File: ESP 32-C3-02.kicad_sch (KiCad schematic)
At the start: 24 parts, among them J3 GSD090012SEU, U2 ESP32-C3-WROOM-02-H4, U3 CP2102N-Axx-xQFN20, U4 W25Q32JVSSIQ, U5 USBLC6-2SC6

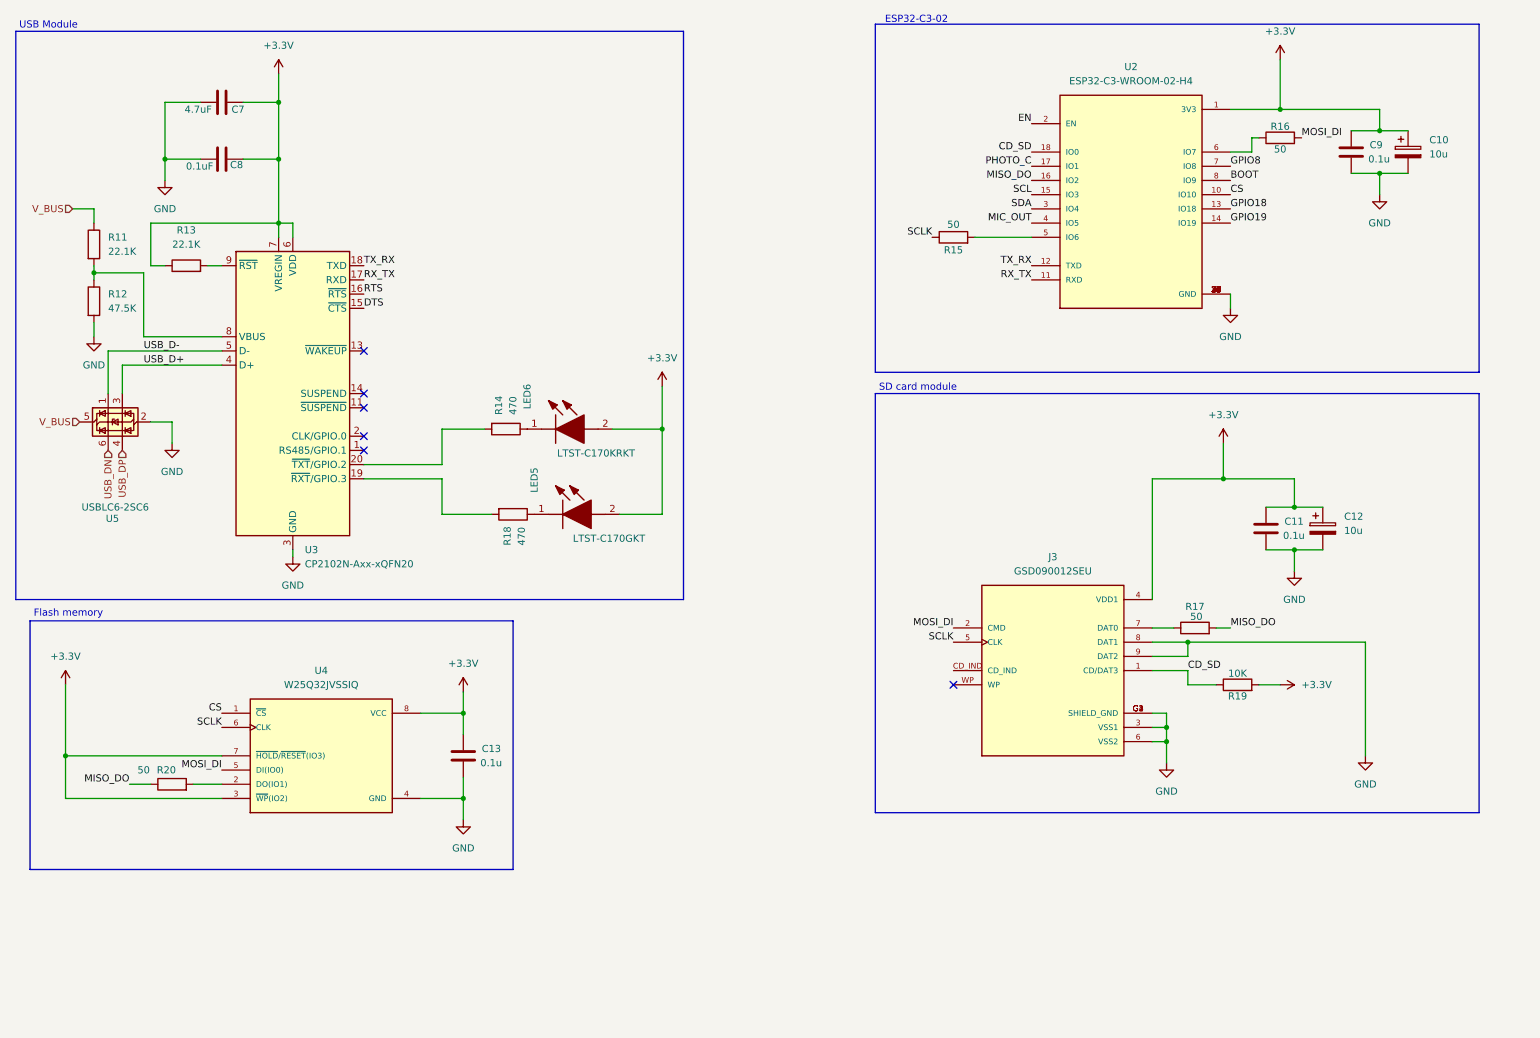
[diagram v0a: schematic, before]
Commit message: test point added to the schematics
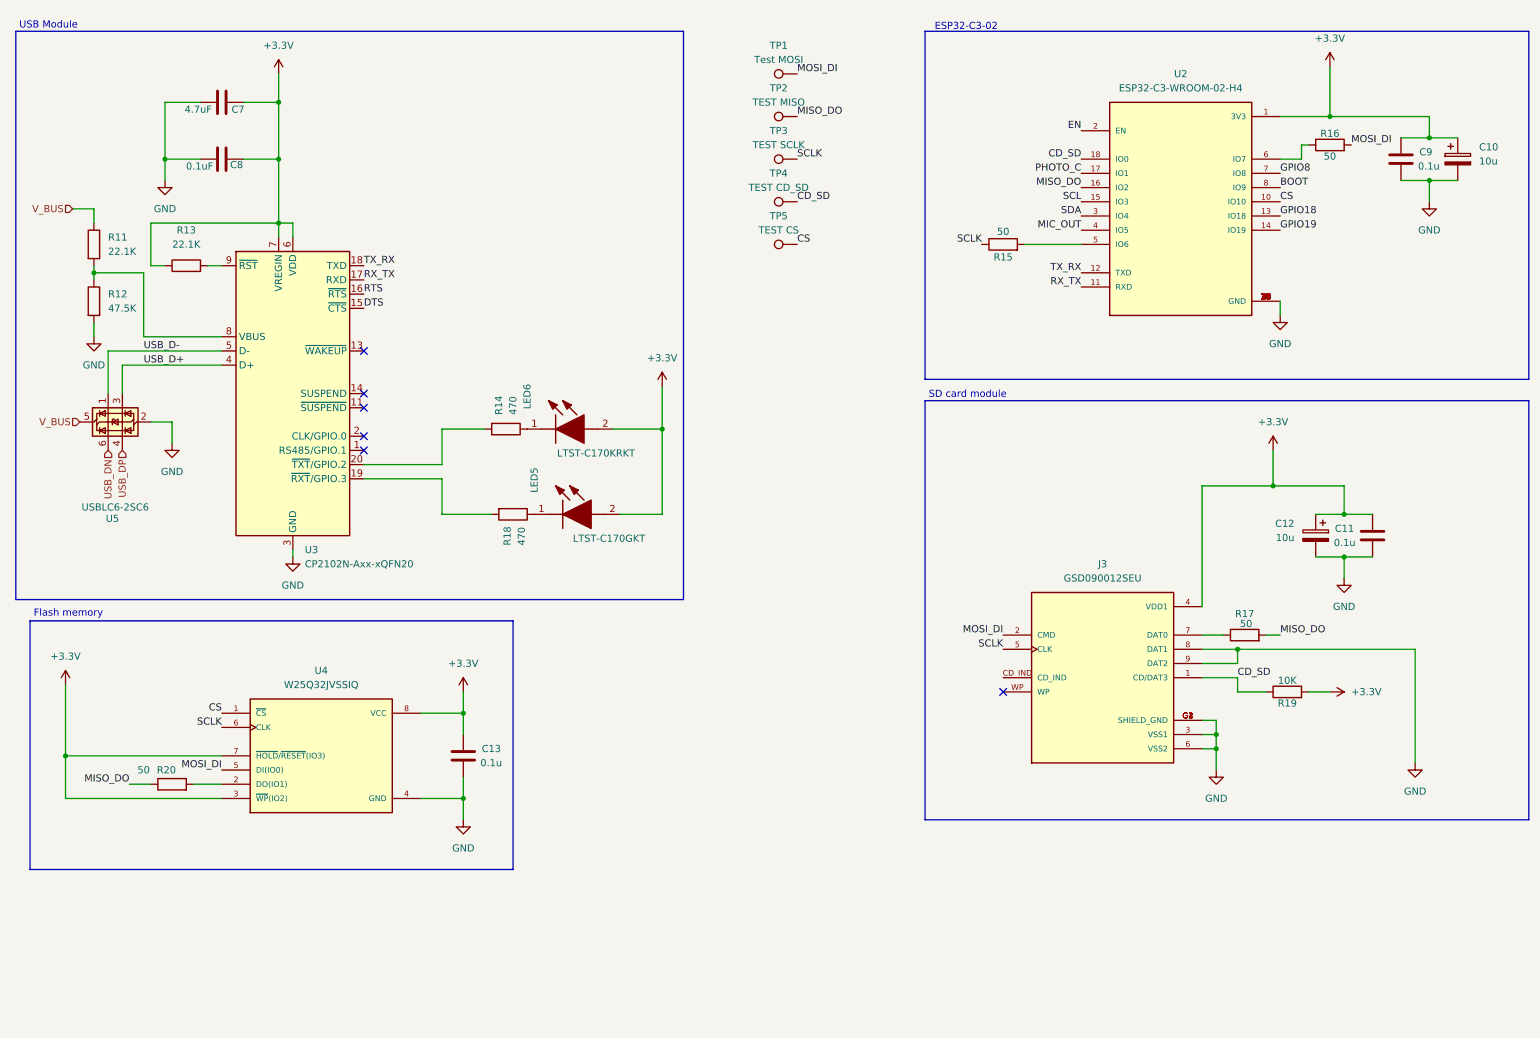
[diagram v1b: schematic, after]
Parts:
- added TP1: Test MOSI, symbol Connector:TestPoint
- added TP2: TEST MISO, symbol Connector:TestPoint
- added TP3: TEST SCLK, symbol Connector:TestPoint
- added TP4: TEST CD_SD, symbol Connector:TestPoint
- added TP5: TEST CS, symbol Connector:TestPoint
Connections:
- net CD_SD: now also TP4.1
- net CS: now also TP5.1
- net MISO_DO: now also TP2.1
- net MOSI_DI: now also TP1.1
- net SCLK: now also TP3.1
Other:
- title: (none) -> ESP 32 C3, USB, and flash memory
- moved on the sheet: C10, C11, C12, C9, J3, R15, R16, R17, R19, U2

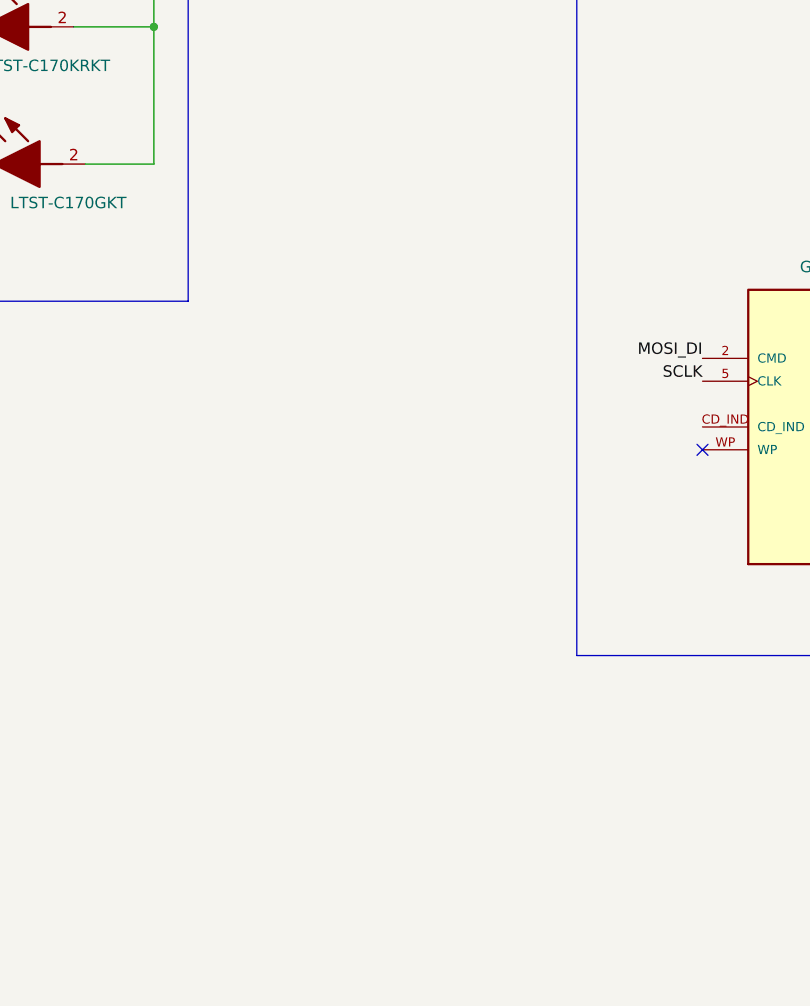
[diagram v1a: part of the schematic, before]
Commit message: BME 280 temperature and humidity sensor
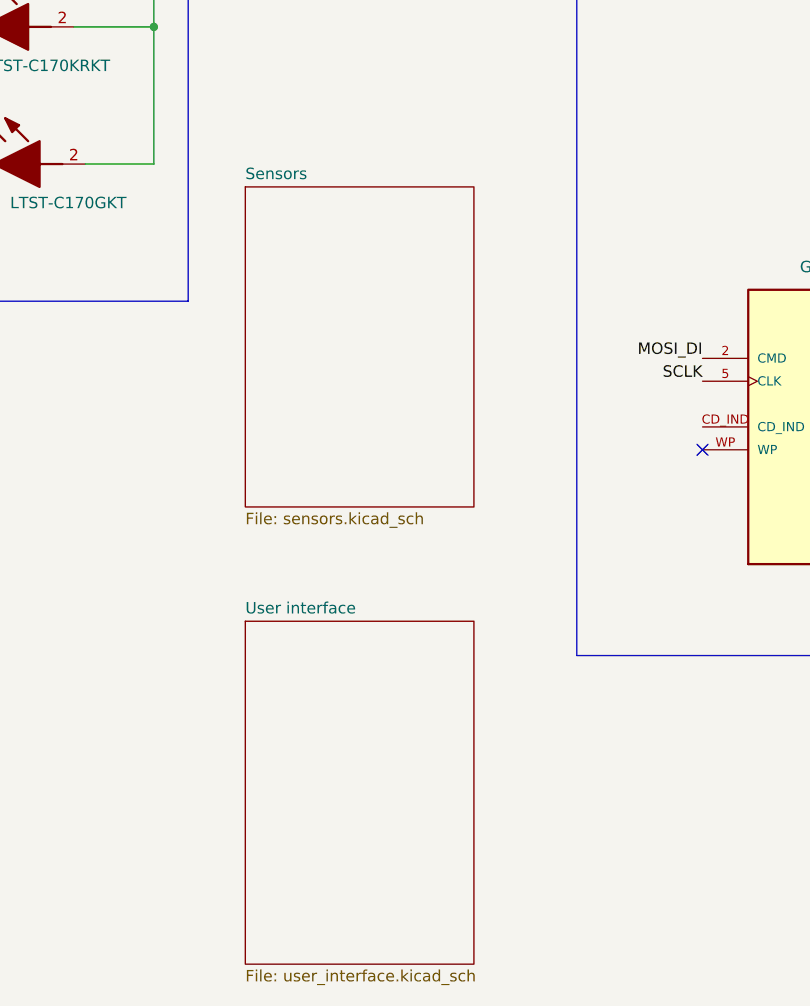
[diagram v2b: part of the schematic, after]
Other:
- added sheet Sensors (sensors.kicad_sch)
- added sheet User interface (user_interface.kicad_sch)
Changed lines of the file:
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@@
+		)
+	)
+	(sheet
+		(at 139.7 105.41)
+		(size 25.4 35.56)
+		(exclude_from_sim no)
+		(in_bom yes)
+		(on_board yes)
+		(dnp no)
+		(fields_autoplaced yes)
+		(stroke
+			(width 0.1524)
+			(type solid)
+			(color 99 255 154 1)
+		)
+		(fill
+			(color 7 255 157 1.0000)
+		)
+		(property "Sheetname" "Sensors"
+			(at 139.7 104.6984 0)
+			(effects
+				(font
+					(size 1.27 1.27)
+				)
+				(justify left bottom)
+			)
+		)
+		(property "Sheetfile" "sensors.kicad_sch"
+			(at 139.7 141.5546 0)
+			(effects
+				(font
+					(size 1.27 1.27)
+				)
+				(justify left top)
+			)
+		)
+		(instances
+			(project "esp32"
+				(path "/3a4906cd-b970-47fd-b3df-3da3a46542f3/ce9639a1-645c-4d9b-b86e-887c0addc46e"
+					(page "3")
+				)
+			)
+		)
+	)
+	(sheet
+		(at 139.7 153.67)
+		(size 25.4 38.1)
+		(exclude_from_sim no)
+		(in_bom yes)
+		(on_board yes)
+		(dnp no)
+		(fields_autoplaced yes)
+		(stroke
+			(width 0.1524)
+			(type solid)
+			(color 255 120 120 1)
+		)
+		(fill
+			(color 255 98 28 1.0000)
+		)
+		(property "Sheetname" "User interface"
+			(at 139.7 152.9584 0)
+			(effects
+				(font
+					(size 1.27 1.27)
+				)
+				(justify left bottom)
+			)
+		)
+		(property "Sheetfile" "user_interface.kicad_sch"
+			(at 139.7 192.3546 0)
+			(effects
+				(font
+					(size 1.27 1.27)
+				)
+				(justify left top)
+			)
+		)
+		(instances
+			(project "esp32"
+				(path "/3a4906cd-b970-47fd-b3df-3da3a46542f3/ce9639a1-645c-4d9b-b86e-887c0addc46e"
+					(page "4")
+				)
+			)
 		)
 	)

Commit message: UI workig
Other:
- sheet Sensors ports: added MIC_OUT, PHOTO_C, SCL, SDA; removed none
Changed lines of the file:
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@@
+			)
+		)
+		(pin "MIC_OUT" output
+			(at 165.1 109.22 0)
+			(effects
+				(font
+					(size 1.27 1.27)
+				)
+				(justify right)
+			)
+		)
+		(pin "PHOTO_C" input
+			(at 165.1 111.76 0)
+			(effects
+				(font
+					(size 1.27 1.27)
+				)
+				(justify right)
+			)
+		)
+		(pin "SCL" input
+			(at 165.1 114.3 0)
+			(effects
+				(font
+					(size 1.27 1.27)
+				)
+				(justify right)
+			)
+		)
+		(pin "SDA" input
+			(at 165.1 116.84 0)
+			(effects
+				(font
+					(size 1.27 1.27)
+				)
+				(justify right)
 			)
 		)

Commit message: latest new dev
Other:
- sheet User interface ports: added BOOT, DTR, EN, GPIO18, GPIO8, GPIO819, RTS, SCL, SDA; removed none

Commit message: next working on that part
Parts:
- C10, C12, C7: footprint (none) -> Footprints:T491A
- C11, C13, C8, C9: footprint (none) -> Capacitor_SMD:C_0805_2012Metric
- J3: footprint GSD090012SEU:AMPHENOL_GSD090012SEU -> Footprints:AMPHENOL_GSD090012SEU
- LED5, LED6: footprint LEDC2012X120N -> Footprints:LEDC2012X120N
- R11, R12, R13, R14, R15, R16, R17, R18, R19, R20: footprint (none) -> Resistor_SMD:R_0805_2012Metric
- TP1, TP2, TP3, TP4, TP5: footprint (none) -> TestPoint:TestPoint_Pad_D1.0mm
- U2: footprint ESP32-C3-WROOM-02-H4:MODULE_ESP32-C3-WROOM-02-H4 -> Footprints:MODULE_ESP32-C3-WROOM-02-H4
- U4: footprint W25Q32JVSSIQ:SOIC127P790X216-8N -> Footprints:SOIC127P790X216-8N
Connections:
- no-connect marks 6 -> 7
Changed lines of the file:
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@@
 	)
 	(no_connect
+		(at 190.5 132.08)
+	)
+	(no_connect
 		(at 76.2 73.66)
 	)
@@
 	(wire
 		(pts
+			(xy 165.1 114.3) (xy 168.91 114.3)
+		)
+		(stroke
+			(width 0)
+			(type default)
+		)
+	)
+	(wire
+		(pts
+			(xy 165.1 116.84) (xy 168.91 116.84)
+		)
+		(stroke
+			(width 0)
+			(type default)
+		)
+	)
+	(wire
+		(pts
 			(xy 63.5 50.8) (xy 60.96 50.8)
 		)
@@
 		)
 	)
+	(label "MIC_OUT"
+		(at 165.1 109.22 0)
+		(effects
+			(font
+				(size 1.27 1.27)
+			)
+			(justify left bottom)
+		)
+	)
 	(label "CS"
 		(at 153.67 54.61 0)
@@
 		)
 	)
+	(label "PHOTO_C"
+		(at 165.1 111.76 0)
+		(effects
+			(font
+				(size 1.27 1.27)
+			)
+			(justify left bottom)
+		)
+	)
 	(label "DTS"
 		(at 76.2 66.04 0)
@@
 		)
 	)
+	(label "SCL"
+		(at 168.91 116.84 0)
+		(effects
+			(font
+				(size 1.27 1.27)
+			)
+			(justify left bottom)
+		)
+	)
 	(label "SCLK"
 		(at 153.67 39.37 0)
@@
 		)
 	)
+	(label "SDA"
+		(at 168.91 114.3 0)
+		(effects
+			(font
+				(size 1.27 1.27)
+			)
+			(justify left bottom)
+		)
+	)
 	(label "TX_RX"
 		(at 204.47 59.69 180)
@@
 			)
 		)
-		(property "Footprint" ""
+		(property "Footprint" "Footprints:T491A"
 			(at 54.61 28.2448 0)
 			(effects
@@
 			)
 		)
-		(property "Footprint" "W25Q32JVSSIQ:SOIC127P790X216-8N"
+		(property "Footprint" "Footprints:SOIC127P790X216-8N"
 			(at 68.58 146.05 0)
 			(effects
@@
 			)
 		)
-		(property "Footprint" ""
+		(property "Footprint" "Resistor_SMD:R_0805_2012Metric"
 			(at 102.87 101.092 90)
 			(effects
@@
 			)
 		)
-		(property "Footprint" ""
+		(property "Footprint" "Resistor_SMD:R_0805_2012Metric"
 			(at 26.162 54.61 90)
 			(effects
@@
 			)
 		)
-		(property "Footprint" ""
+		(property "Footprint" "Footprints:T491A"
 			(at 245.4148 110.49 0)
 			(effects
@@
 			)
 		)
-		(property "Footprint" "GSD090012SEU:AMPHENOL_GSD090012SEU"
+		(property "Footprint" "Footprints:AMPHENOL_GSD090012SEU"
 			(at 208.28 132.08 0)
 			(effects
@@
 			)
 		)
-		(property "Footprint" ""
+		(property "Footprint" "Resistor_SMD:R_0805_2012Metric"
 			(at 44.45 60.198 90)
 			(effects
@@
 			)
 		)
-		(property "Footprint" ""
+		(property "Footprint" "TestPoint:TestPoint_Pad_D1.0mm"
 			(at 153.67 41.91 0)
 			(effects
@@
 			)
 		)
-		(property "Footprint" ""
+		(property "Footprint" "Resistor_SMD:R_0805_2012Metric"
 			(at 190.5 56.388 90)
 			(effects
@@
 			)
 		)
-		(property "Footprint" ""
+		(property "Footprint" "TestPoint:TestPoint_Pad_D1.0mm"
 			(at 153.67 49.53 0)
 			(effects
@@
 			)
 		)
-		(property "Footprint" ""
+		(property "Footprint" "Capacitor_SMD:C_0805_2012Metric"
 			(at 255.5748 110.49 0)
 			(effects
@@
 			)
 		)
-		(property "Footprint" ""
+		(property "Footprint" "Capacitor_SMD:C_0805_2012Metric"
 			(at 262.5852 43.18 0)
 			(effects
@@
 			)
 		)
-		(property "Footprint" "ESP32-C3-WROOM-02-H4:MODULE_ESP32-C3-WROOM-02-H4"
+		(property "Footprint" "Footprints:MODULE_ESP32-C3-WROOM-02-H4"
 			(at 222.25 49.53 0)
 			(effects
@@
 			)
 		)
-		(property "Footprint" ""
+		(property "Footprint" "Footprints:T491A"
 			(at 272.7452 43.18 0)
 			(effects
@@
 			)
 		)
-		(property "Footprint" ""
+		(property "Footprint" "Resistor_SMD:R_0805_2012Metric"
 			(at 26.162 64.77 90)
 			(effects
@@
 			)
 		)
-		(property "Footprint" ""
+		(property "Footprint" "TestPoint:TestPoint_Pad_D1.0mm"
 			(at 153.67 26.67 0)
 			(effects
@@
 			)
 		)
-		(property "Footprint" "LEDC2012X120N"
+		(property "Footprint" "Footprints:LEDC2012X120N"
 			(at 119.38 196.52 0)
 			(effects
@@
 			)
 		)
-		(property "Footprint" ""
+		(property "Footprint" "Resistor_SMD:R_0805_2012Metric"
 			(at 233.68 126.238 90)
 			(effects
@@
 			)
 		)
-		(property "Footprint" "LEDC2012X120N"
+		(property "Footprint" "Footprints:LEDC2012X120N"
 			(at 118.11 181.28 0)
 			(effects
@@
 			)
 		)
-		(property "Footprint" ""
+		(property "Footprint" "Resistor_SMD:R_0805_2012Metric"
 			(at 248.92 38.608 90)
 			(effects
@@
 			)
 		)
-		(property "Footprint" ""
+		(property "Footprint" "Capacitor_SMD:C_0805_2012Metric"
 			(at 54.61 38.4048 0)
 			(effects
@@
 			)
 		)
-		(property "Footprint" ""
+		(property "Footprint" "TestPoint:TestPoint_Pad_D1.0mm"
 			(at 153.67 19.05 0)
 			(effects
@@
 			)
 		)
-		(property "Footprint" ""
+		(property "Footprint" "TestPoint:TestPoint_Pad_D1.0mm"
 			(at 153.67 34.29 0)
 			(effects
@@
 			)
 		)
-		(property "Footprint" ""
+		(property "Footprint" "Resistor_SMD:R_0805_2012Metric"
 			(at 241.3 136.398 90)
 			(effects
@@
 			)
 		)
-		(property "Footprint" ""
+		(property "Footprint" "Capacitor_SMD:C_0805_2012Metric"
 			(at 94.9452 149.86 0)
 			(effects
@@
 			)
 		)
-		(property "Footprint" ""
+		(property "Footprint" "Resistor_SMD:R_0805_2012Metric"
 			(at 101.6 85.852 90)
 			(effects
@@
 			)
 		)
-		(property "Footprint" ""
+		(property "Footprint" "Resistor_SMD:R_0805_2012Metric"
 			(at 41.91 152.908 90)
 			(effects
@@
 			)
 		)
-		(pin "PHOTO_C" input
+		(pin "PHOTO_C" output
 			(at 165.1 111.76 0)
 			(effects
